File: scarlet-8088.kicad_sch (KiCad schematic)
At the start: 9 parts

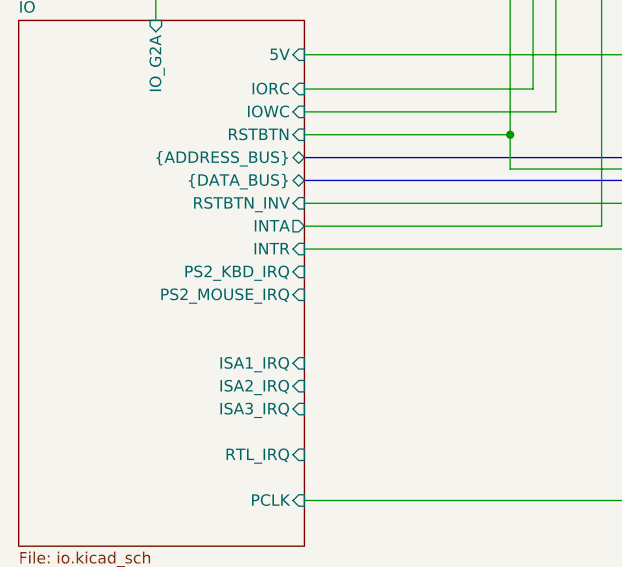
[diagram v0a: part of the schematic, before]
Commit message: Added compatible RJ45 Ethernet
Signed-off-by: Lucy Mielke <user@domain.tld>
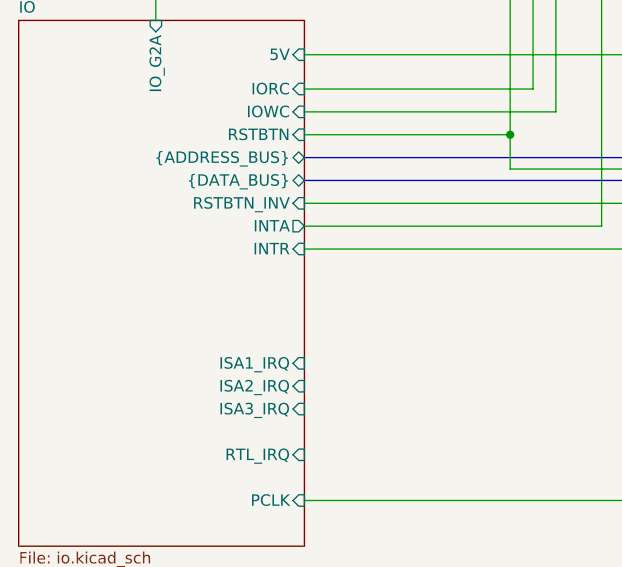
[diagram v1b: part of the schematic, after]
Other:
- sheet IO ports: added none; removed PS2_KBD_IRQ, PS2_MOUSE_IRQ
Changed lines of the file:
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@@
-			)
-		)
-		(pin "PS2_KBD_IRQ" input
-			(at 48.26 86.36 0)
-			(effects
-				(font
-					(size 1.27 1.27)
-				)
-				(justify right)
-			)
-		)
-		(pin "PS2_MOUSE_IRQ" input
-			(at 48.26 88.9 0)
-			(effects
-				(font
-					(size 1.27 1.27)
-				)
-				(justify right)
 			)
 		)

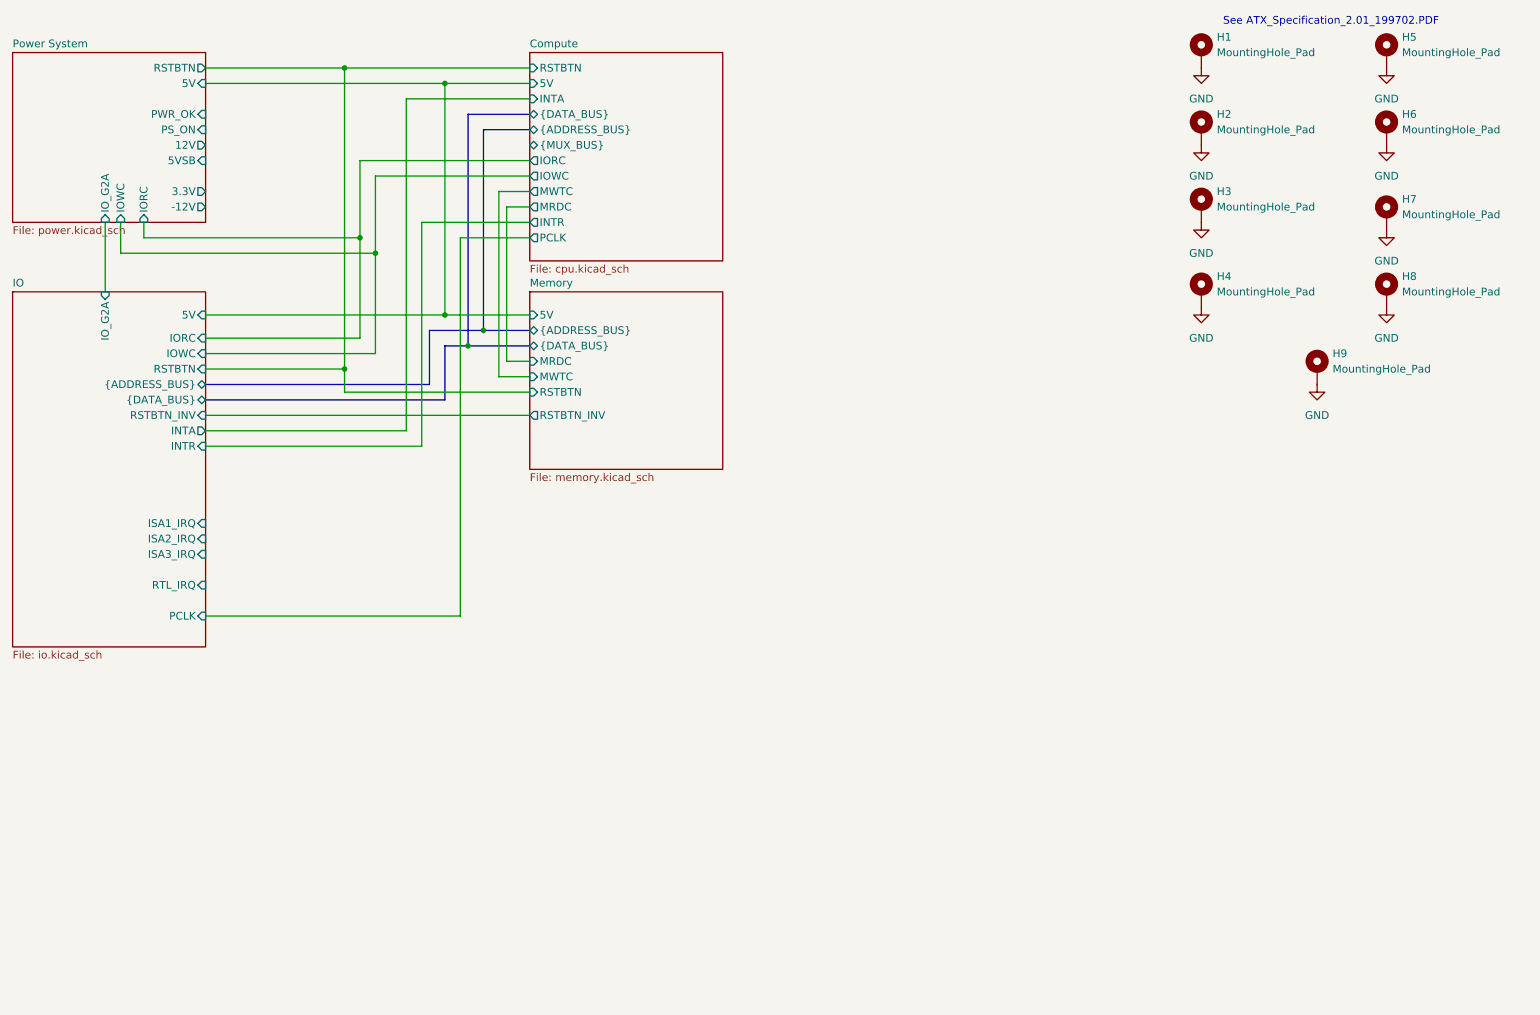
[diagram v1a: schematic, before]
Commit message: IDE controller/connector
Signed-off-by: Lucy Mielke <user@domain.tld>
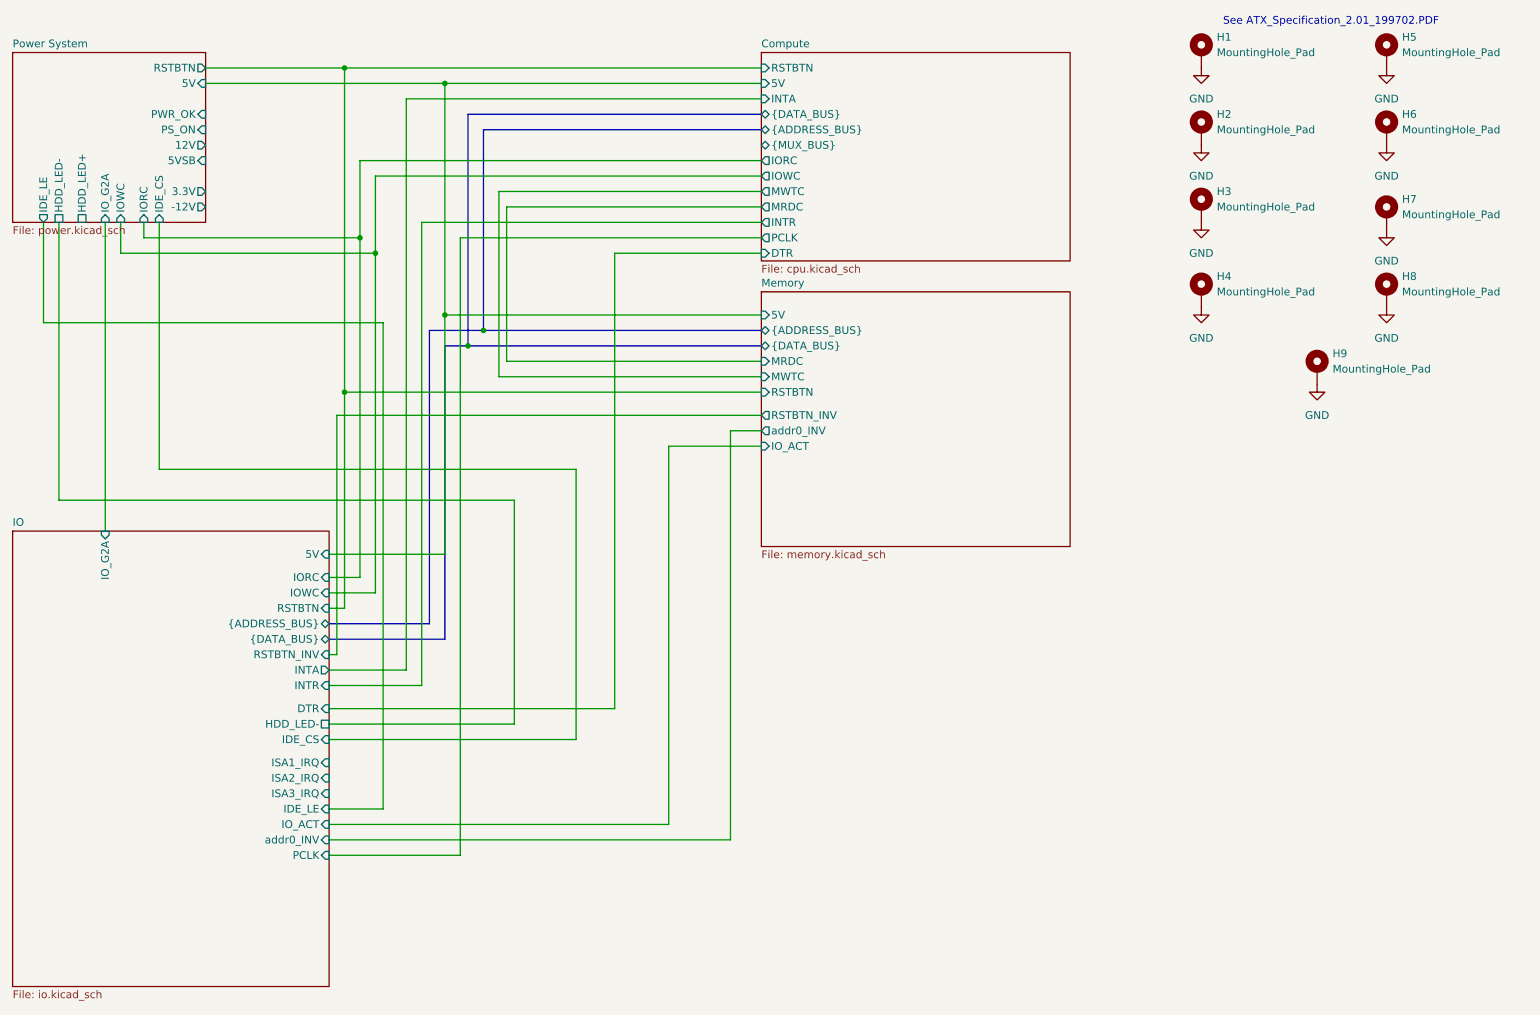
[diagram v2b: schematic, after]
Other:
- sheet Compute ports: added DTR; removed none
- sheet IO ports: added DTR, HDD_LED-, IDE_CS, IDE_LE, IO_ACT, addr0_INV; removed RTL_IRQ
- sheet Memory ports: added IO_ACT, addr0_INV; removed none
- sheet Power System ports: added HDD_LED+, HDD_LED-, IDE_CS, IDE_LE; removed none

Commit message: ISA card slots, schematic cleanup
Signed-off-by: Lucy Mielke <user@domain.tld>
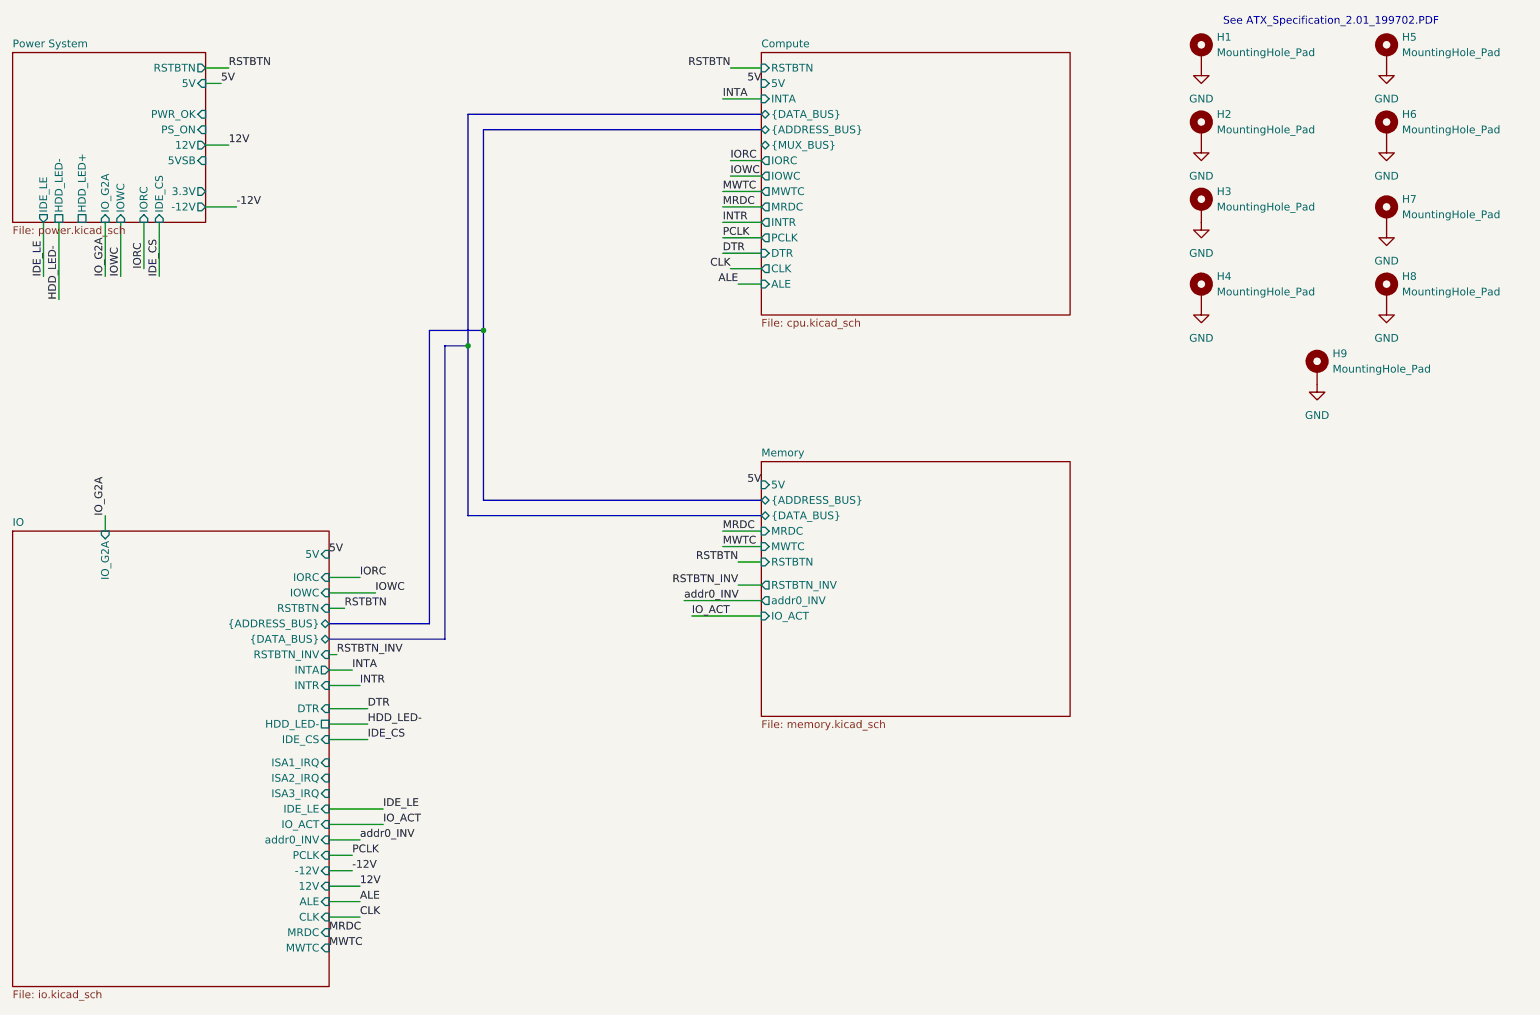
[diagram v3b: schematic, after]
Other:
- sheet Compute ports: added ALE, CLK; removed none
- sheet IO ports: added -12V, 12V, ALE, CLK, MRDC, MWTC; removed none

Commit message: Fix ERC errors
Signed-off-by: Lucy Mielke <user@domain.tld>
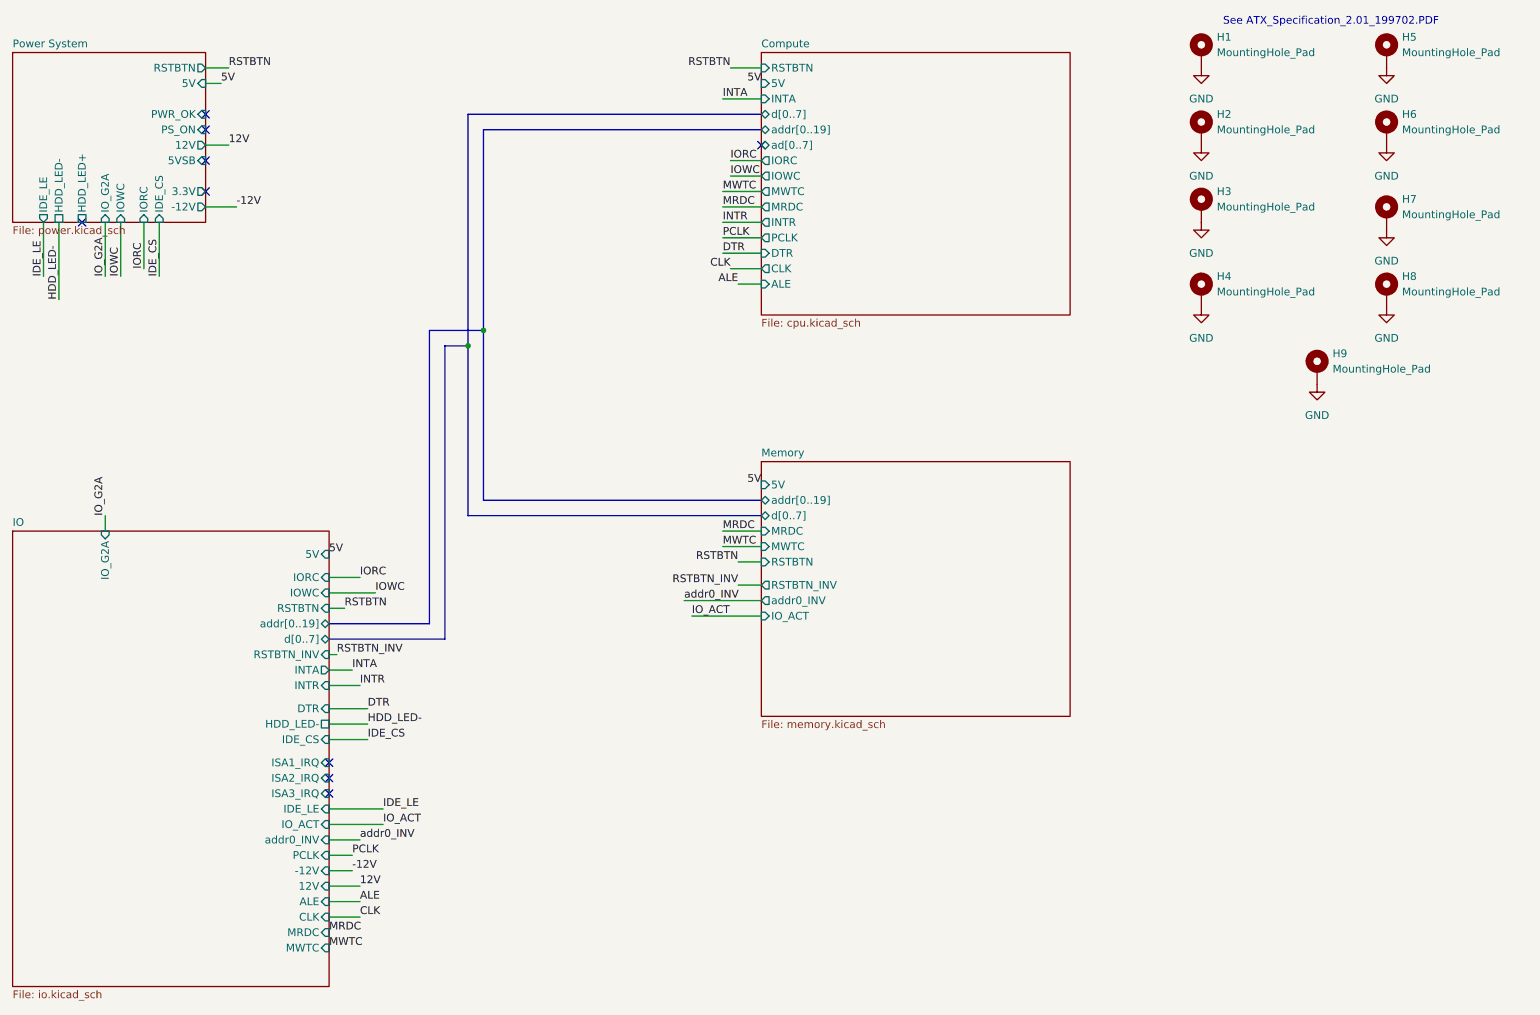
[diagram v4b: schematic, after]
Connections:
- no-connect marks 0 -> 9
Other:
- sheet Compute ports: added ad[0..7], addr[0..19], d[0..7]; removed {ADDRESS_BUS}, {DATA_BUS}, {MUX_BUS}
- sheet IO ports: added addr[0..19], d[0..7]; removed {ADDRESS_BUS}, {DATA_BUS}
- sheet Memory ports: added addr[0..19], d[0..7]; removed {ADDRESS_BUS}, {DATA_BUS}
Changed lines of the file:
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@@
 		(color 0 0 0 0)
 	)
+	(no_connect
+		(at 68.58 140.97)
+	)
+	(no_connect
+		(at 48.26 31.75)
+	)
+	(no_connect
+		(at 48.26 41.91)
+	)
+	(no_connect
+		(at 139.7 34.29)
+	)
+	(no_connect
+		(at 48.26 29.21)
+	)
+	(no_connect
+		(at 68.58 135.89)
+	)
+	(no_connect
+		(at 68.58 138.43)
+	)
+	(no_connect
+		(at 48.26 36.83)
+	)
+	(no_connect
+		(at 27.94 46.99)
+	)
 	(wire
 		(pts
@@
 		)
 	)
+	(bus
+		(pts
+			(xy 93.98 31.75) (xy 139.7 31.75)
+		)
+		(stroke
+			(width 0)
+			(type default)
+		)
+	)
 	(wire
 		(pts
@@
 		)
 	)
-	(bus
-		(pts
-			(xy 139.7 31.75) (xy 93.98 31.75)
-		)
-		(stroke
-			(width 0)
-			(type default)
-		)
-	)
 	(wire
 		(pts
@@
 			)
 		)
-		(pin "{ADDRESS_BUS}" bidirectional
+		(pin "addr[0..19]" bidirectional
 			(at 139.7 92.71 180)
 			(effects
@@
 			)
 		)
-		(pin "{DATA_BUS}" bidirectional
+		(pin "d[0..7]" bidirectional
 			(at 139.7 95.25 180)
 			(effects
@@
 			)
 		)
-		(pin "{ADDRESS_BUS}" bidirectional
+		(pin "addr[0..19]" bidirectional
 			(at 68.58 113.03 0)
 			(effects
@@
 			)
 		)
-		(pin "{DATA_BUS}" bidirectional
+		(pin "d[0..7]" bidirectional
 			(at 68.58 115.57 0)
 			(effects
@@
 			)
 		)
-		(pin "{ADDRESS_BUS}" bidirectional
+		(pin "addr[0..19]" bidirectional
 			(at 139.7 31.75 180)
 			(effects
@@
 			)
 		)
-		(pin "{DATA_BUS}" bidirectional
+		(pin "d[0..7]" bidirectional
 			(at 139.7 29.21 180)
 			(effects
@@
 			)
 		)
-		(pin "{MUX_BUS}" bidirectional
+		(pin "ad[0..7]" bidirectional
 			(at 139.7 34.29 180)
 			(effects
